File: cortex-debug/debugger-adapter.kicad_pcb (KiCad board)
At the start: 2 copper layers, 17.3 x 10.7 mm, 4 parts

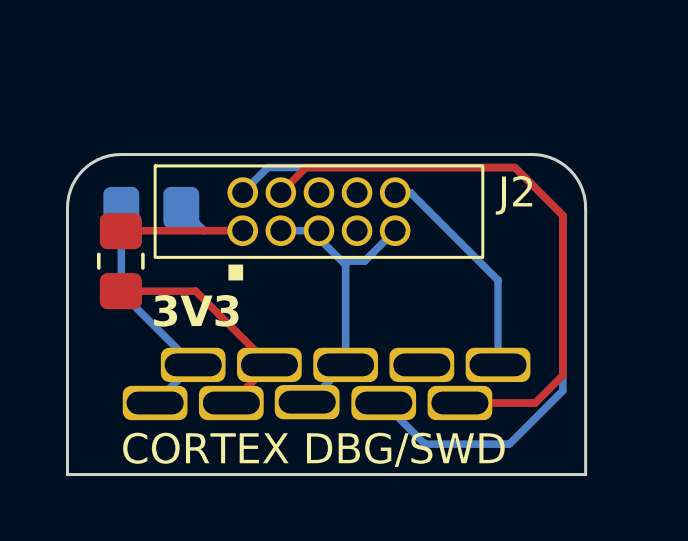
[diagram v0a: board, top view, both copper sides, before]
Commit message: Update stlink connector footprint to a better part
 - No more jankily soldering in an IDC connector, found an actual connector that works
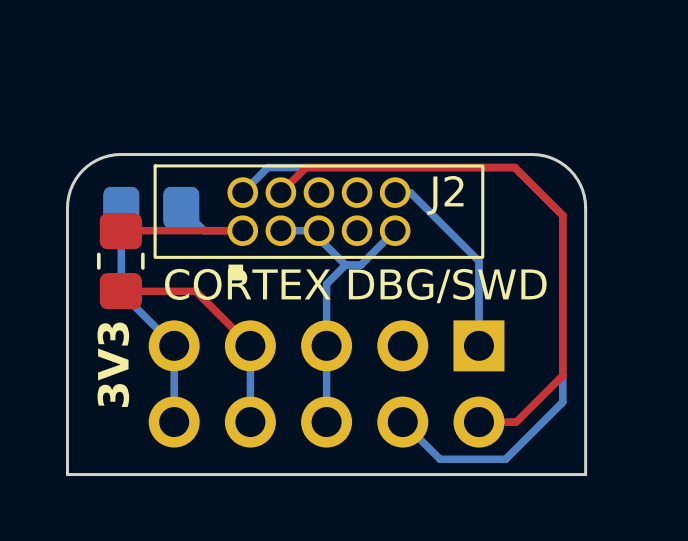
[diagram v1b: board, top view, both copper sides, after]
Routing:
- net /RST: track 7.46 -> 6.56 mm

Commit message: Replace solder jumpers with selector switch
I got annoyed that my debugger was set for the wrong
voltage or set to provide power when I didn't want it to, so
small revision to add a selector switch. Makes the board a little bigger
but whatever.
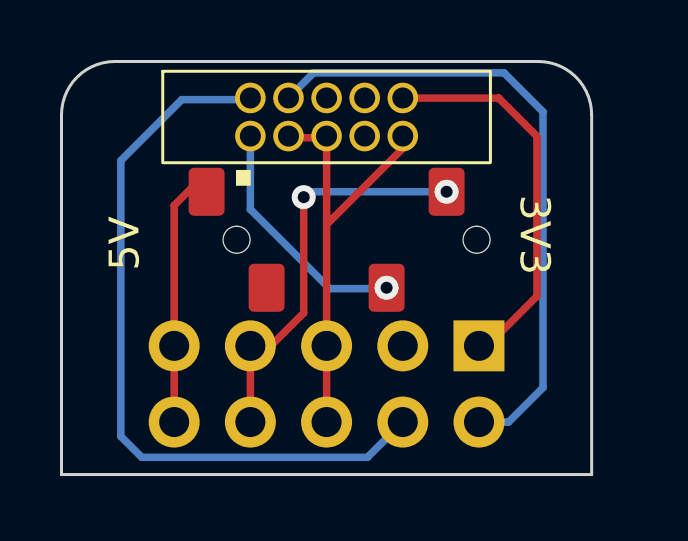
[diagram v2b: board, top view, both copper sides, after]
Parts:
- removed R1, R2: 0, Resistor_SMD:R_0805_2012Metric_Pad1.20x1.40mm_HandSolder
- added S1: ~, common-components:Slide_SP3T, F.Cu at (41.7, 35.9)
- moved J2 3.16 mm to (41.7, 31.8)
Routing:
- net /RST: track 6.56 -> 12.9 mm
- net Net-(J1-3.3V-Pad7): track 7.61 -> 13.5 mm, vias 0 -> 2
- net GND: track 10.4 -> 14.8 mm
- net VCC: track 6.43 -> 8.90 mm, vias 0 -> 1
- net /SWCLK: track 19.2 -> 21.2 mm
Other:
- board size 17.3 x 10.7 mm -> 17.7 x 13.8 mm
- board text removed: "JLCJLCJLCJLC"
